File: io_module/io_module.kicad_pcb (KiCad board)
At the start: 2 copper layers, 67.3 x 20 mm, 9 parts, among them J1 8P, J2 10P, J3 8P, J4 10P, J5 EA, J6 EB, U1 MCP23S17_ML

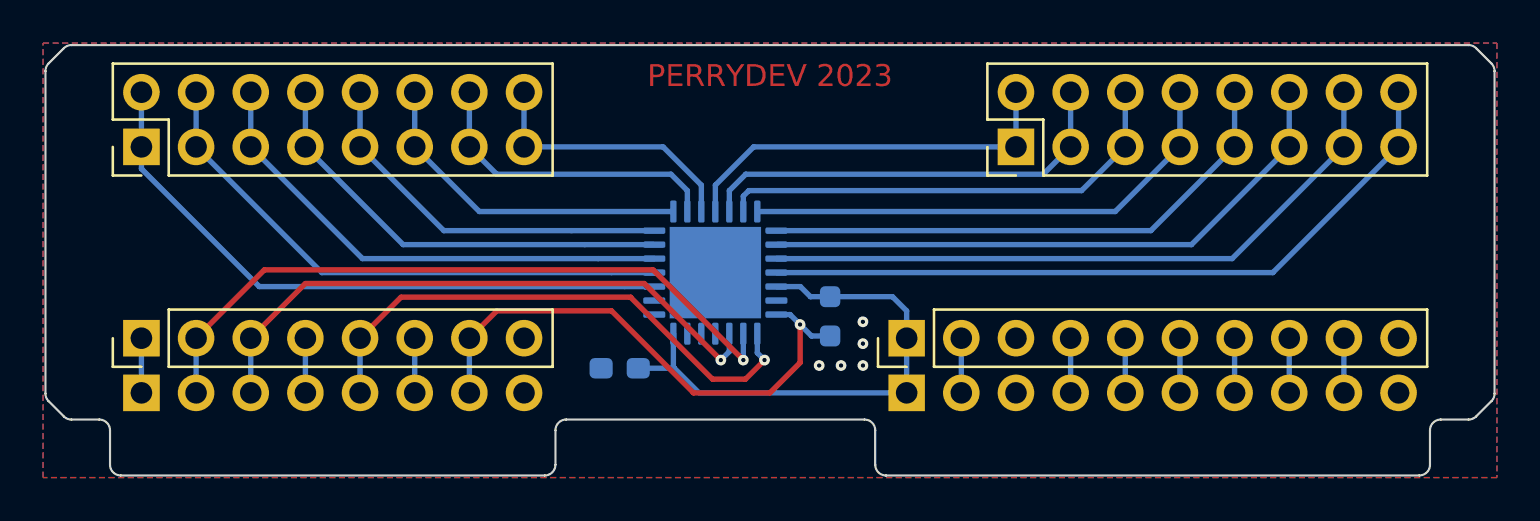
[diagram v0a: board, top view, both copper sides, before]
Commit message: io module silkscreen
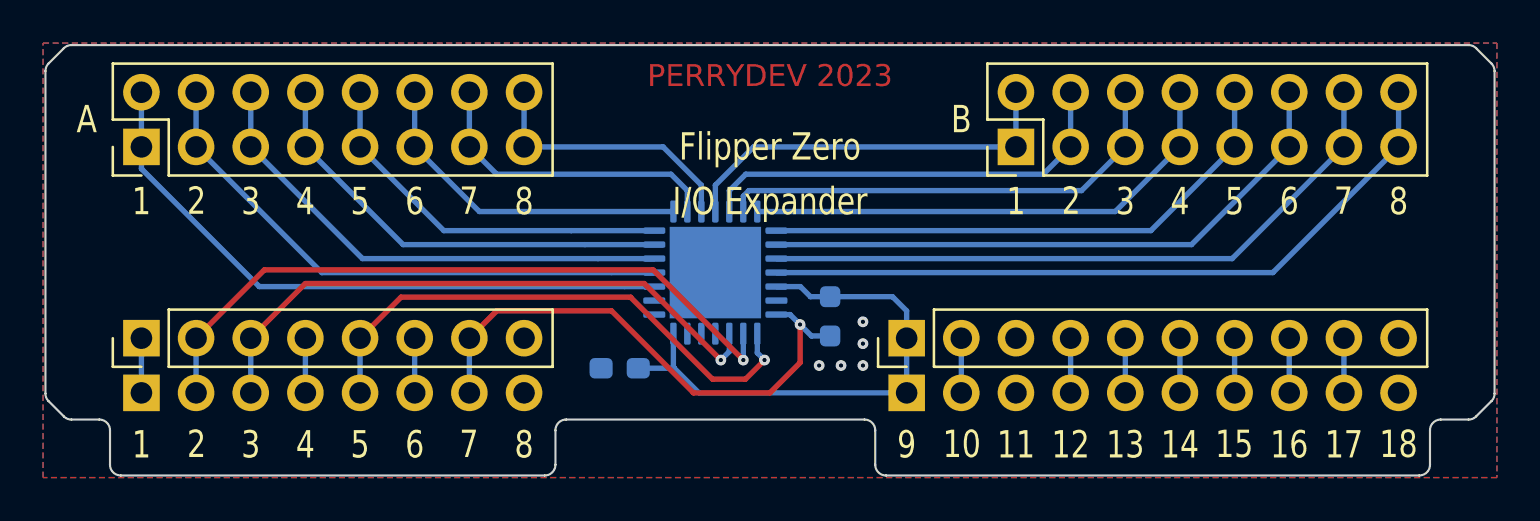
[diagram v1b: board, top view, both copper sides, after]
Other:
- board text added: "1"
- board text added: "10"
- board text added: "11"
- board text added: "12"
- board text added: "13"
- board text added: "14"
- board text added: "15"
- board text added: "16"
- board text added: "17"
- board text added: "18"
- board text added: "2"
- board text added: "3"
- board text added: "4"
- board text added: "5"
- board text added: "6"
- board text added: "7"
- board text added: "8"
- board text added: "9"
- board text added: "A"
- board text added: "B"
- board text added: "Flipper Zero"
- board text added: "I/O Expander"
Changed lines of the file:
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@@
     (effects (font (size 1.016 1.016) (thickness 0.254)))
+  )
+  (gr_text "8" (at 140.97 54.61) (layer "F.SilkS")
+    (effects (font (size 1.27 1.016) (thickness 0.2032)))
+  )
+  (gr_text "5" (at 133.35 65.913) (layer "F.SilkS")
+    (effects (font (size 1.27 1.016) (thickness 0.2032)))
+  )
+  (gr_text "4" (at 130.81 54.61) (layer "F.SilkS")
+    (effects (font (size 1.27 1.016) (thickness 0.2032)))
+  )
+  (gr_text "13" (at 168.91 65.913) (layer "F.SilkS")
+    (effects (font (size 1.27 1.016) (thickness 0.2032)))
+  )
+  (gr_text "4" (at 171.45 54.61) (layer "F.SilkS")
+    (effects (font (size 1.27 1.016) (thickness 0.2032)))
+  )
+  (gr_text "3" (at 128.27 65.913) (layer "F.SilkS")
+    (effects (font (size 1.27 1.016) (thickness 0.2032)))
+  )
+  (gr_text "Flipper Zero" (at 152.4 52.07) (layer "F.SilkS")
+    (effects (font (size 1.27 1.016) (thickness 0.2032)))
+  )
+  (gr_text "B" (at 161.29 50.8) (layer "F.SilkS")
+    (effects (font (size 1.27 1.016) (thickness 0.2032)))
+  )
+  (gr_text "6" (at 176.53 54.61) (layer "F.SilkS")
+    (effects (font (size 1.27 1.016) (thickness 0.2032)))
+  )
+  (gr_text "9" (at 158.75 65.913) (layer "F.SilkS")
+    (effects (font (size 1.27 1.016) (thickness 0.2032)))
+  )
+  (gr_text "6" (at 135.89 54.61) (layer "F.SilkS")
+    (effects (font (size 1.27 1.016) (thickness 0.2032)))
+  )
+  (gr_text "I/O Expander" (at 152.4 54.61) (layer "F.SilkS")
+    (effects (font (size 1.27 1.016) (thickness 0.2032)))
+  )
+  (gr_text "7" (at 138.411155 65.893451) (layer "F.SilkS")
+    (effects (font (size 1.27 1.016) (thickness 0.2032)))
+  )
+  (gr_text "4" (at 130.81 65.913) (layer "F.SilkS")
+    (effects (font (size 1.27 1.016) (thickness 0.2032)))
+  )
+  (gr_text "1" (at 123.19 65.913) (layer "F.SilkS")
+    (effects (font (size 1.27 1.016) (thickness 0.2032)))
+  )
+  (gr_text "14" (at 171.45 65.913) (layer "F.SilkS")
+    (effects (font (size 1.27 1.016) (thickness 0.2032)))
+  )
+  (gr_text "1" (at 123.19 54.61) (layer "F.SilkS")
+    (effects (font (size 1.27 1.016) (thickness 0.2032)))
+  )
+  (gr_text "17" (at 179.07 65.913) (layer "F.SilkS")
+    (effects (font (size 1.27 1.016) (thickness 0.2032)))
+  )
+  (gr_text "7" (at 179.051155 54.590451) (layer "F.SilkS")
+    (effects (font (size 1.27 1.016) (thickness 0.2032)))
+  )
+  (gr_text "1" (at 163.83 54.61) (layer "F.SilkS")
+    (effects (font (size 1.27 1.016) (thickness 0.2032)))
+  )
+  (gr_text "5" (at 133.35 54.61) (layer "F.SilkS")
+    (effects (font (size 1.27 1.016) (thickness 0.2032)))
+  )
+  (gr_text "15" (at 173.971155 65.893451) (layer "F.SilkS")
+    (effects (font (size 1.27 1.016) (thickness 0.2032)))
+  )
+  (gr_text "10" (at 161.312055 65.893451) (layer "F.SilkS")
+    (effects (font (size 1.27 1.016) (thickness 0.2032)))
+  )
+  (gr_text "2" (at 125.752055 54.590451) (layer "F.SilkS")
+    (effects (font (size 1.27 1.016) (thickness 0.2032)))
+  )
+  (gr_text "A" (at 120.65 50.8) (layer "F.SilkS")
+    (effects (font (size 1.27 1.016) (thickness 0.2032)))
+  )
+  (gr_text "2" (at 166.392055 54.590451) (layer "F.SilkS")
+    (effects (font (size 1.27 1.016) (thickness 0.2032)))
+  )
+  (gr_text "2" (at 125.752055 65.893451) (layer "F.SilkS")
+    (effects (font (size 1.27 1.016) (thickness 0.2032)))
+  )
+  (gr_text "6" (at 135.89 65.913) (layer "F.SilkS")
+    (effects (font (size 1.27 1.016) (thickness 0.2032)))
+  )
+  (gr_text "3" (at 128.27 54.61) (layer "F.SilkS")
+    (effects (font (size 1.27 1.016) (thickness 0.2032)))
+  )
+  (gr_text "16" (at 176.53 65.913) (layer "F.SilkS")
+    (effects (font (size 1.27 1.016) (thickness 0.2032)))
+  )
+  (gr_text "7" (at 138.411155 54.590451) (layer "F.SilkS")
+    (effects (font (size 1.27 1.016) (thickness 0.2032)))
+  )
+  (gr_text "3" (at 168.91 54.61) (layer "F.SilkS")
+    (effects (font (size 1.27 1.016) (thickness 0.2032)))
+  )
+  (gr_text "12" (at 166.37 65.913) (layer "F.SilkS")
+    (effects (font (size 1.27 1.016) (thickness 0.2032)))
+  )
+  (gr_text "18" (at 181.606058 65.893451) (layer "F.SilkS")
+    (effects (font (size 1.27 1.016) (thickness 0.2032)))
+  )
+  (gr_text "11" (at 163.83 65.913) (layer "F.SilkS")
+    (effects (font (size 1.27 1.016) (thickness 0.2032)))
+  )
+  (gr_text "8" (at 181.61 54.61) (layer "F.SilkS")
+    (effects (font (size 1.27 1.016) (thickness 0.2032)))
+  )
+  (gr_text "5" (at 173.99 54.61) (layer "F.SilkS")
+    (effects (font (size 1.27 1.016) (thickness 0.2032)))
+  )
+  (gr_text "8" (at 140.97 65.913) (layer "F.SilkS")
+    (effects (font (size 1.27 1.016) (thickness 0.2032)))
   )
   (segment (start 123.19 63.5) (end 123.19 60.96) (width 0.25) (layer "B.Cu") (net 1))

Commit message: io expansion board r2
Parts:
- moved R1 11.0 mm to (144.4, 62.0), turned to -90 degrees
- moved C1 9.10 mm to (154.2, 59.9), turned to -90 degrees
- moved U1 1.02 mm to (148.8, 57.9)
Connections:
- net /PA6 renamed /MISO
- net /PA7 renamed /MOSI
- R1 pad 1: /PC3 -> /PB2
- U1 pad 7: /PC3 -> /PB2
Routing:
- net /PB2: track 2.54 -> 25.8 mm, vias 0 -> 2
- net /PC3: track 25.3 -> 2.54 mm, vias 1 -> 0
- net +3.3V: track 24.9 -> 29.8 mm, vias 0 -> 2
- net /PB3: track 25.4 -> 24.1 mm
- net /MOSI: track 32.2 -> 30.9 mm
- net /MISO: track 28.3 -> 27.1 mm
- net /EA4: track 17.8 -> 16.8 mm
- net /EA3: track 20.6 -> 19.6 mm
- net /EA2: track 23.4 -> 22.4 mm
- net /EA1: track 26.3 -> 25.2 mm
- net /EA0: track 29.7 -> 28.6 mm
- net /EB0: track 18.5 -> 19.5 mm
- net /EA7: track 12.7 -> 11.7 mm
- net /EB7: track 33.9 -> 34.9 mm
- net /EB6: track 31.1 -> 32.1 mm
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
